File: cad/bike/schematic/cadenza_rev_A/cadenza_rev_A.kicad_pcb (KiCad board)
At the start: 2 copper layers, 90 x 60 mm, 60 parts, among them J2 USB_C_Receptacle, J3 Conn_01x02, J4 Conn_01x02, J5 Conn_01x02, Q1 BC547, SW1 SW_Slide_DPDT, SW2 SW_Push, SW3 SW_Push, U1 TLC5916, U10 HDSP-A151, U11 TLC5916, U12 HDSP-A151, U13 STM32F105RCTx, U14 LT1962-3.3, U15 TLC5916, U2 HDSP-A151, U3 TLC5916, U4 HDSP-A151, U5 TLC5916, U6 HDSP-A151, U7 TLC5916, U8 HDSP-A151, U9 TLC5916

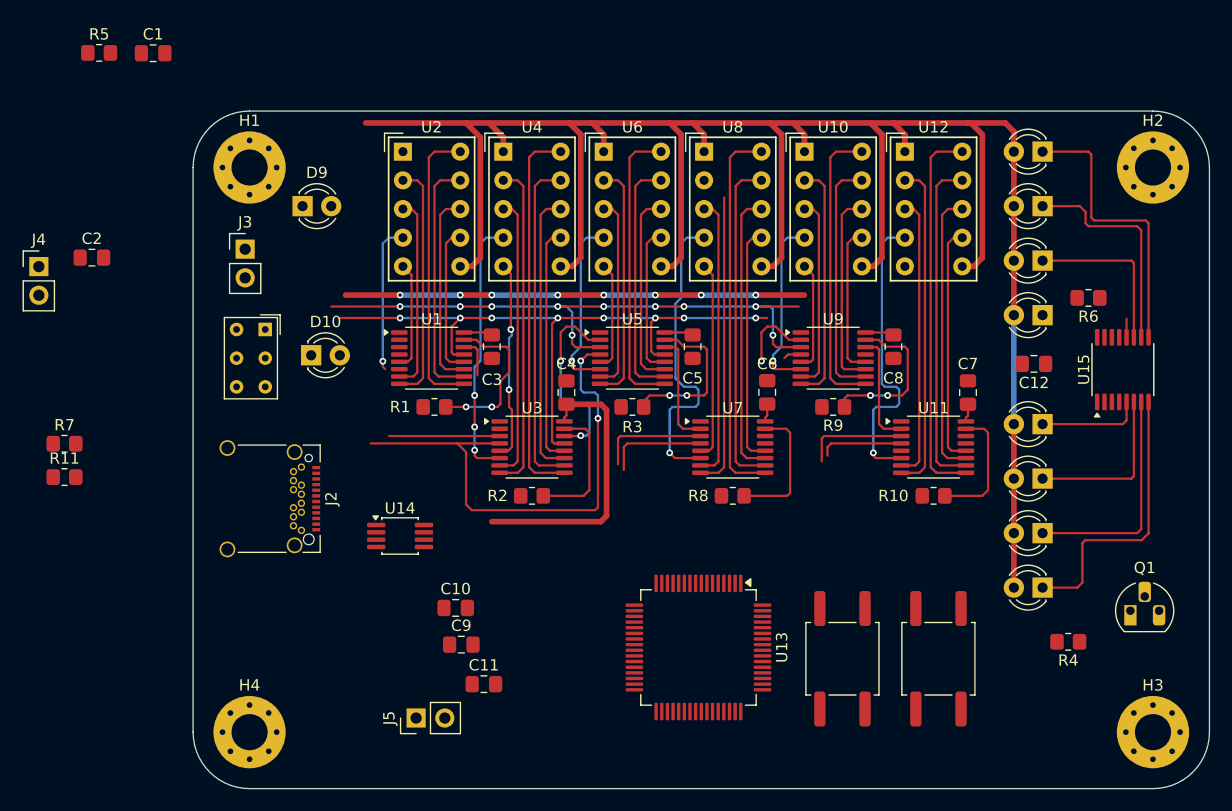
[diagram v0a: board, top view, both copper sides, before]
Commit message: added the debug interface
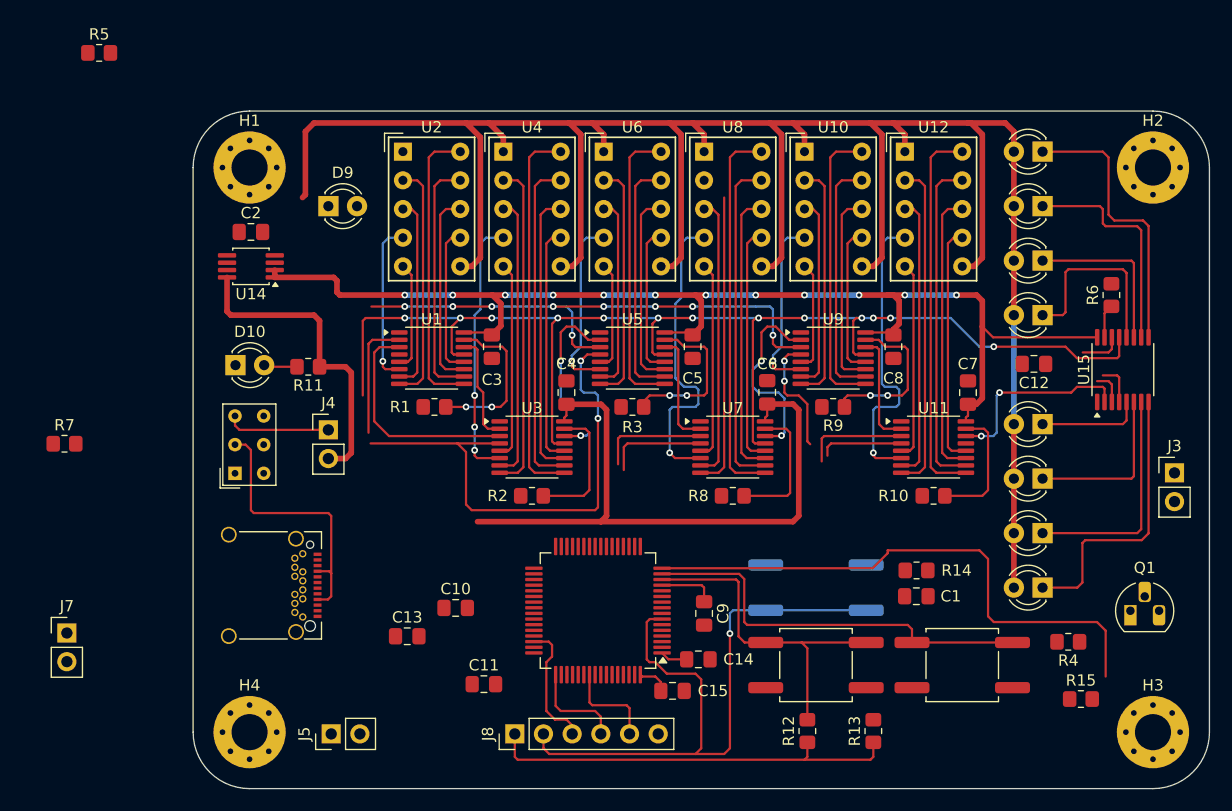
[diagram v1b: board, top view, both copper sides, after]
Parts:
- added C13: 10nF, Capacitor_SMD:C_0805_2012Metric_Pad1.18x1.45mm_HandSolder, F.Cu at (69.0, 96.5)
- added C14: 100nF, Capacitor_SMD:C_0805_2012Metric_Pad1.18x1.45mm_HandSolder, F.Cu at (94.7, 98.6)
- added C15: 100nF, Capacitor_SMD:C_0805_2012Metric_Pad1.18x1.45mm_HandSolder, F.Cu at (92.5, 101.3)
- added J7: Conn_01x02, Connector_PinHeader_2.54mm:PinHeader_1x02_P2.54mm_Vertical, F.Cu at (38.8, 96.2)
- added J8: Conn_01x06, Connector_PinHeader_2.54mm:PinHeader_1x06_P2.54mm_Vertical, F.Cu at (78.5, 105.2)
- added R12: R_US, Resistor_SMD:R_0805_2012Metric_Pad1.20x1.40mm_HandSolder, F.Cu at (104.4, 104.9)
- added R13: R_US, Resistor_SMD:R_0805_2012Metric_Pad1.20x1.40mm_HandSolder, F.Cu at (110.2, 104.9)
- added R14: 10k, Resistor_SMD:R_0805_2012Metric_Pad1.20x1.40mm_HandSolder, F.Cu at (114.1, 90.7)
- added R15: 1k, Resistor_SMD:R_0805_2012Metric_Pad1.20x1.40mm_HandSolder, F.Cu at (128.6, 102.1)
- added SW4: SW_Push, Button_Switch_SMD:SW_Push_1P1T_NO_CK_KSC6xxG, B.Cu at (105.2, 92.2)
- R5: value R_US -> 10k
- moved J3 84.6 mm to (136.9, 82.0)
- moved C1 82.9 mm to (114.0, 93.0)
- moved J4 29.4 mm to (62.0, 78.2)
- moved U14 27.3 mm to (55.1, 63.8), turned to 180 degrees
- moved R11 23.7 mm to (60.2, 72.6), turned to 180 degrees
- moved C9 21.7 mm to (95.2, 94.5), turned to -90 degrees
- moved C2 14.3 mm to (55.1, 60.7)
- moved SW1 13.0 mm to (53.7, 82.1), turned to 90 degrees
- moved U13 9.48 mm to (85.9, 94.2), turned to 180 degrees
- moved J2 7.67 mm to (56.0, 92.0)
- moved J5 7.65 mm to (62.2, 105.2)
- moved D10 6.76 mm to (53.8, 72.5)
- moved SW2 2.41 mm to (105.2, 99.1), turned to 180 degrees
- moved D9 2.29 mm to (62.0, 58.4)
- moved SW3 2.18 mm to (118.1, 99.1), turned to 180 degrees
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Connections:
- C1 pad 1: +3.3V -> /~{RESET}
- D1 pad 2: +5VL -> +5V
- D2 pad 2: +5VL -> +5V
- D3 pad 2: +5VL -> +5V
- D4 pad 2: +5VL -> +5V
- D5 pad 2: +5VL -> +5V
- D6 pad 2: +5VL -> +5V
- D7 pad 2: +5VL -> +5V
- D8 pad 2: +5VL -> +5V
- Q1 pad 2: unconnected-(Q1-B-Pad2) -> Net-(Q1-B)
- SW2 pad 1: unconnected-(SW2-Pad1) -> GND
- SW2 pad 2: unconnected-(SW2-Pad2) -> /PB_{1}
- SW3 pad 1: unconnected-(SW3-Pad1) -> GND
- SW3 pad 2: unconnected-(SW3-Pad2) -> /PB_{2}
- U10 pad 1: +5VL -> +5V
- U10 pad 6: +5VL -> +5V
- U12 pad 1: +5VL -> +5V
- U12 pad 6: +5VL -> +5V
- U13 pad 14: unconnected-(U13-PA0-Pad14) -> /PB_{1}
- U13 pad 15: unconnected-(U13-PA1-Pad15) -> /PB_{2}
- U13 pad 16: unconnected-(U13-PA2-Pad16) -> Net-(U13-PA2)
- U13 pad 46: unconnected-(U13-PA13-Pad46) -> /SW_DIO
- U13 pad 49: unconnected-(U13-PA14-Pad49) -> /SW_CLK
- U13 pad 55: unconnected-(U13-PB3-Pad55) -> /SW_O
- U13 pad 7: +3.3V -> /~{RESET}
- U14 pad 2: unconnected-(U14-SENSE-Pad2) -> +3.3V
- U14 pad 3: unconnected-(U14-BYP-Pad3) -> Net-(U14-BYP)
- U14 pad 5: unconnected-(U14-~{SHDN}-Pad5) -> +5V
- U2 pad 1: +5VL -> +5V
- U2 pad 6: +5VL -> +5V
- U4 pad 1: +5VL -> +5V
- U4 pad 6: +5VL -> +5V
- U6 pad 1: +5VL -> +5V
- U6 pad 6: +5VL -> +5V
- U8 pad 1: +5VL -> +5V
- U8 pad 6: +5VL -> +5V
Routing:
- net +5V: track 0.00 -> 239.7 mm
- net +5VL: track 200.1 -> 0.00 mm
- net +3.3V: track 37.2 -> 212.6 mm, vias 0 -> 12
- net /~{RESET}: track 0.00 -> 59.5 mm, vias 0 -> 1
- net Net-(U1-~{OE}(ED2)): track 59.1 -> 115.2 mm, vias 8 -> 13
- net Net-(U13-PA2): track 0.00 -> 50.1 mm
- net (no net): track 40.6 -> 0.00 mm, vias 8 -> 0
- net /PB_{2}: track 0.00 -> 36.5 mm
- net /PB_{1}: track 0.00 -> 30.3 mm
- net Net-(J2-VBUS-PadA4): track 0.00 -> 24.0 mm
- net Net-(U11-~{OUT0}): track 0.00 -> 17.5 mm
- net Net-(U11-SDO): track 0.00 -> 17.4 mm, vias 0 -> 2
- net Net-(D4-K): track 1.64 -> 17.0 mm
- net Net-(U1-LE(ED1)): track 63.3 -> 76.1 mm, vias 2 -> 4
- net /SW_DIO: track 0.00 -> 11.4 mm
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
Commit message: routing backup
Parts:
- added C16: 100nF, Capacitor_SMD:C_0805_2012Metric_Pad1.18x1.45mm_HandSolder, F.Cu at (104.4, 104.6)
- added C17: 100nF, Capacitor_SMD:C_0805_2012Metric_Pad1.18x1.45mm_HandSolder, F.Cu at (118.1, 104.7)
- added C18: 100nF, Capacitor_SMD:C_0805_2012Metric_Pad1.18x1.45mm_HandSolder, F.Cu at (67.3, 101.1)
- added C19: 100nF, Capacitor_SMD:C_0805_2012Metric_Pad1.18x1.45mm_HandSolder, F.Cu at (92.8, 87.9)
- added R16: 330, Resistor_SMD:R_0805_2012Metric_Pad1.20x1.40mm_HandSolder, F.Cu at (63.2, 62.2)
- R12, R13, R7: value R_US -> 4.7k
- moved R5 59.8 mm to (74.7, 94.7)
- moved C13 35.6 mm to (59.2, 62.2), turned to 90 degrees
- moved R7 33.9 mm to (64.8, 101.1), turned to -90 degrees
- moved J7 31.6 mm to (70.4, 94.0), turned to -90 degrees
- moved R15 10.2 mm to (134.9, 94.0), turned to 90 degrees
- moved C12 7.20 mm to (129.0, 66.8), turned to 90 degrees
- moved C10 7.14 mm to (78.0, 88.6), turned to 180 degrees
- moved R11 6.20 mm to (55.1, 69.1), turned to 0 degrees
- moved Q1 5.77 mm to (134.4, 88.6), turned to 180 degrees
- moved J4 5.68 mm to (59.4, 73.2), turned to 180 degrees
- moved R13 5.59 mm to (115.8, 104.6)
- moved J3 5.57 mm to (131.8, 84.3), turned to 90 degrees
- moved R4 5.06 mm to (131.6, 94.0), turned to -90 degrees
- moved C2 4.59 mm to (53.6, 65.0)
- moved J8 3.81 mm to (74.7, 105.2)
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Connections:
- D9 pad 2: unconnected-(D9-A-Pad2) -> Net-(D9-A)
- J5 pad 1: +3.3V -> Net-(J5-Pin_1)
- R7 pad 1: Net-(J5-Pin_2) -> +3.3V
- R7 pad 2: GND -> Net-(J5-Pin_1)
- SW1 pad 2: Net-(J2-VBUS-PadA4) -> unconnected-(SW1-B-Pad2)
- SW1 pad 3: Net-(J4-Pin_1) -> unconnected-(SW1-C-Pad3)
- SW1 pad 5: unconnected-(SW1-B-Pad5) -> Net-(J2-VBUS-PadA4)
- SW1 pad 6: unconnected-(SW1-C-Pad6) -> Net-(J4-Pin_1)
- U1 pad 13: Net-(U1-~{OE}(ED2)) -> /~{LED_OUTPUT_EN}
- U1 pad 4: Net-(U1-LE(ED1)) -> /LED_LATCH_EN
- U11 pad 13: Net-(U1-~{OE}(ED2)) -> /~{LED_OUTPUT_EN}
- U11 pad 4: Net-(U1-LE(ED1)) -> /LED_LATCH_EN
- U13 pad 20: unconnected-(U13-PA4-Pad20) -> /LED_LATCH_EN
- U13 pad 33: unconnected-(U13-PB12-Pad33) -> /WARNING_LED
- U13 pad 35: unconnected-(U13-PB14-Pad35) -> /~{LED_OUTPUT_EN}
- U13 pad 40: unconnected-(U13-PC9-Pad40) -> Net-(J5-Pin_2)
- U15 pad 13: Net-(U1-~{OE}(ED2)) -> /~{LED_OUTPUT_EN}
- U15 pad 4: Net-(U1-LE(ED1)) -> /LED_LATCH_EN
- U3 pad 13: Net-(U1-~{OE}(ED2)) -> /~{LED_OUTPUT_EN}
- U3 pad 4: Net-(U1-LE(ED1)) -> /LED_LATCH_EN
- U5 pad 13: Net-(U1-~{OE}(ED2)) -> /~{LED_OUTPUT_EN}
- U5 pad 4: Net-(U1-LE(ED1)) -> /LED_LATCH_EN
- U7 pad 13: Net-(U1-~{OE}(ED2)) -> /~{LED_OUTPUT_EN}
- U7 pad 4: Net-(U1-LE(ED1)) -> /LED_LATCH_EN
- U9 pad 13: Net-(U1-~{OE}(ED2)) -> /~{LED_OUTPUT_EN}
- U9 pad 4: Net-(U1-LE(ED1)) -> /LED_LATCH_EN
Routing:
- net /~{LED_OUTPUT_EN}: track 0.00 -> 159.3 mm, vias 0 -> 14
- net /LED_LATCH_EN: track 0.00 -> 141.7 mm, vias 0 -> 9
- net Net-(U1-~{OE}(ED2)): track 115.2 -> 0.00 mm, vias 13 -> 0
- net +3.3V: track 212.6 -> 323.4 mm
- net Net-(U1-LE(ED1)): track 76.1 -> 0.00 mm, vias 4 -> 0
- net /SPI_CLK: track 90.6 -> 165.9 mm, vias 9 -> 14
- net /WARNING_LED: track 0.00 -> 41.3 mm, vias 0 -> 2
- net /SPI_MOSI: track 10.7 -> 39.6 mm, vias 0 -> 2
- net Net-(J7-Pin_1): track 0.00 -> 26.4 mm, vias 0 -> 2
- net +5V: track 239.7 -> 265.3 mm
- net Net-(J5-Pin_2): track 0.00 -> 23.4 mm, vias 0 -> 2
- net /PB_{2}: track 36.5 -> 45.5 mm
- net /~{RESET}: track 59.5 -> 51.8 mm
- net Net-(Q1-B): track 0.00 -> 4.56 mm
- net Net-(Q1-E): track 0.00 -> 4.46 mm
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
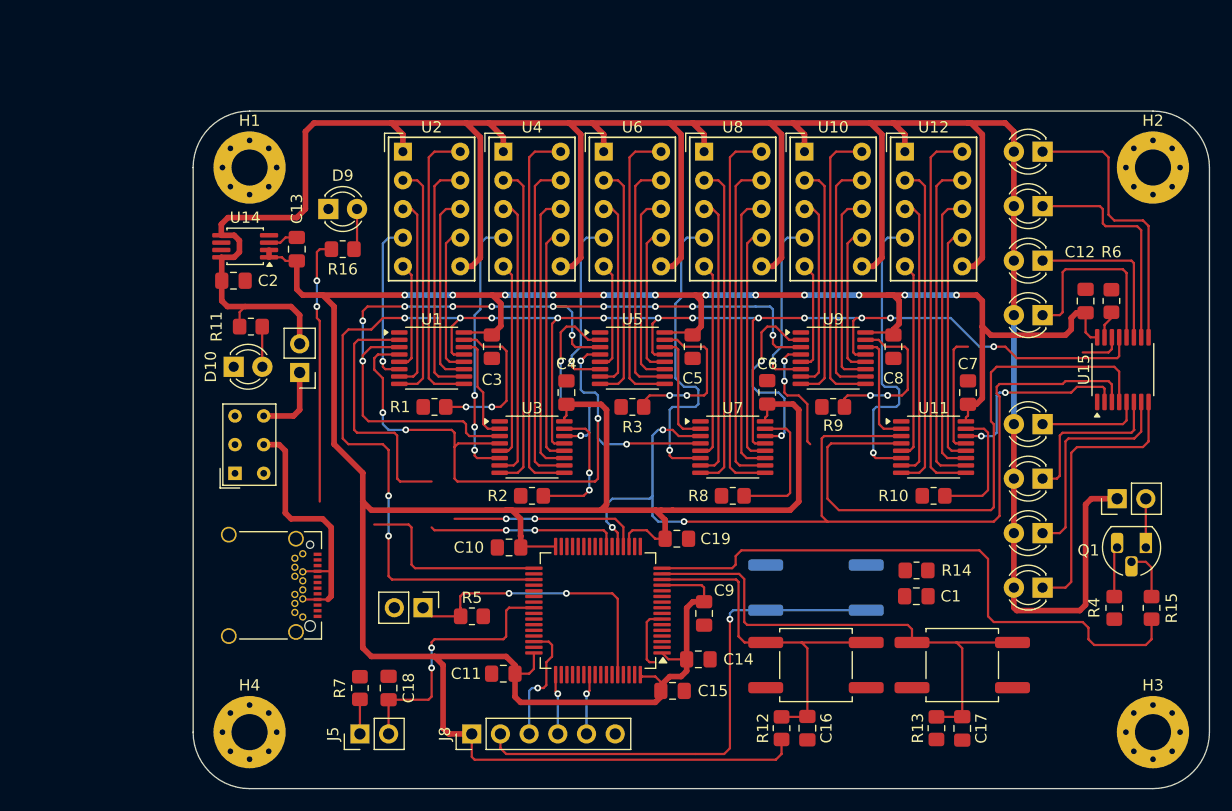
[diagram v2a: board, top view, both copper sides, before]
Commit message: finalised ground plane most of the routing done
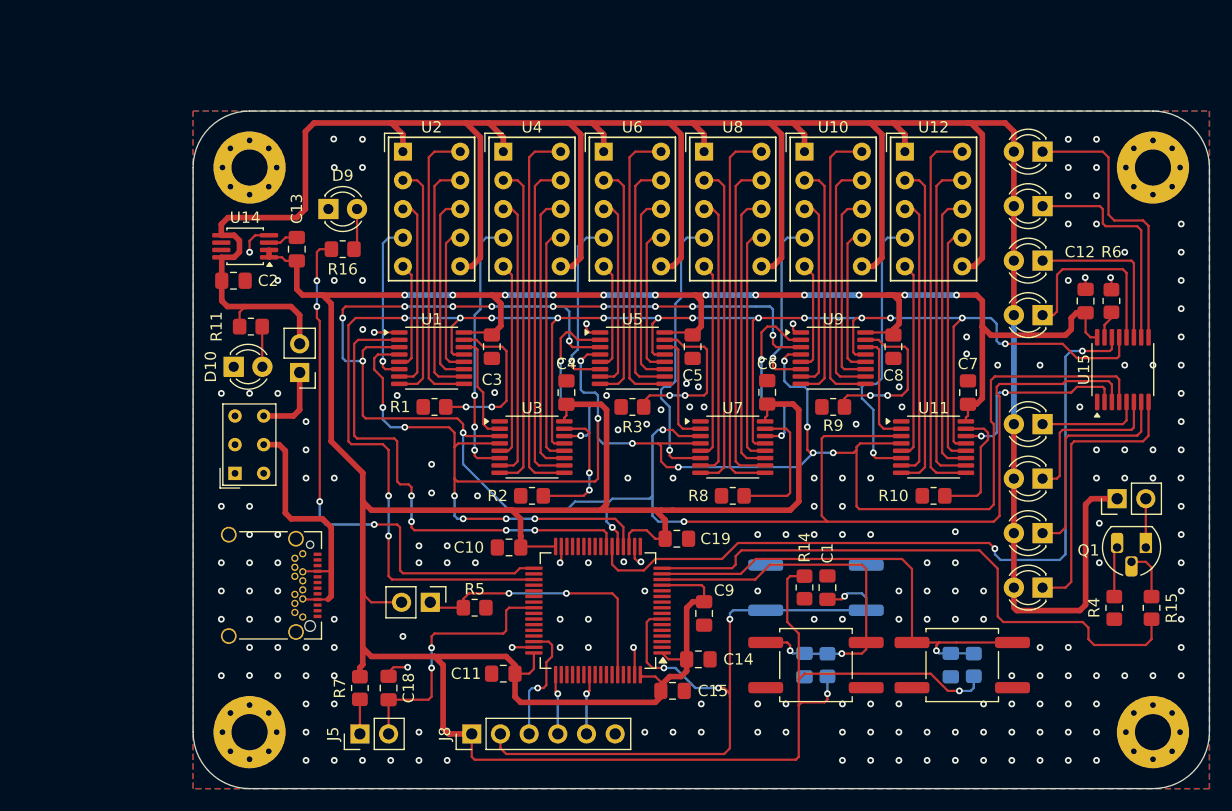
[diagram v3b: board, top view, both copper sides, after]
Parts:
- C16, C17, R12, R13: moved to B.Cu
- moved R14 10.0 mm to (104.1, 92.2), turned to -90 degrees
- moved C1 7.91 mm to (106.2, 92.2), turned to 90 degrees
- moved R12 6.91 mm to (106.2, 99.1)
- moved R13 6.50 mm to (119.1, 99.0)
- moved C17 5.70 mm to (117.1, 99.1)
- moved C16 5.59 mm to (104.1, 99.1)
- moved J7 0.80 mm to (71.0, 93.5)
- moved R5 0.80 mm to (74.9, 94.0)
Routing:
- net /SPI_MISO: track 3.75 -> 67.0 mm, vias 0 -> 2
- net +3.3V: track 323.4 -> 370.1 mm, vias 12 -> 14
- net /SPI_CLK: track 165.9 -> 187.3 mm, vias 14 -> 15
- net GND: track 0.00 -> 20.5 mm, vias 0 -> 200
- net /LED_LATCH_EN: track 141.7 -> 159.5 mm, vias 9 -> 14
- net /~{RESET}: track 51.8 -> 65.6 mm, vias 1 -> 4
- net /WARNING_LED: track 41.3 -> 48.5 mm, vias 2 -> 4
- net /SPI_MOSI: track 39.6 -> 43.5 mm, vias 2 -> 4
- net /PB_{1}: track 32.3 -> 35.6 mm, vias 0 -> 2
- net /PB_{2}: track 45.5 -> 42.7 mm, vias 0 -> 1
- net Net-(U7-~{OUT1}): track 27.7 -> 25.2 mm
- net /~{LED_OUTPUT_EN}: track 159.3 -> 161.6 mm, vias 14 -> 15
- net Net-(U11-~{OUT1}): track 26.8 -> 25.4 mm
- net Net-(J7-Pin_1): track 26.4 -> 25.5 mm
- net Net-(U7-SDO): track 17.4 -> 16.6 mm
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- added copper zone on B.Cu, net GND
- added copper zone on F.Cu, net GND

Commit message: added final touches, no more nets to route
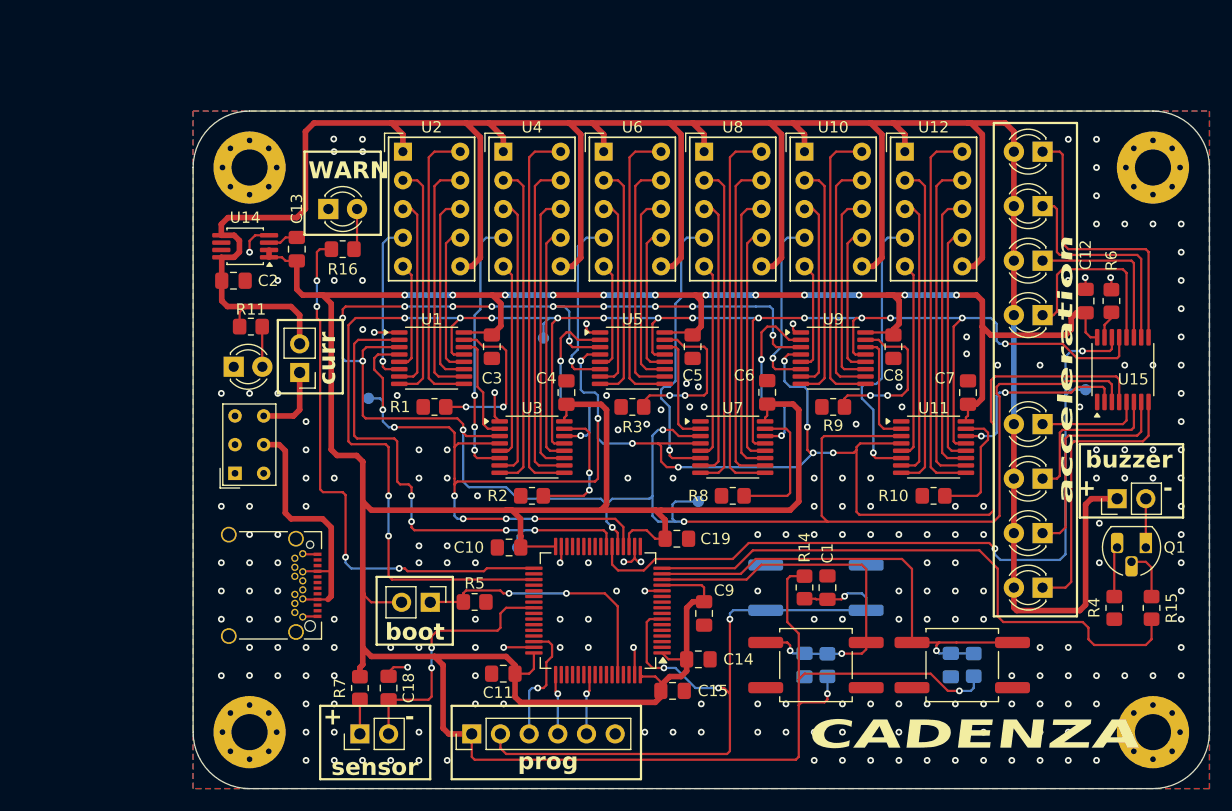
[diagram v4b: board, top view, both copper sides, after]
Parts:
- added TP1: TestPoint, TestPoint:TestPoint_Pad_D1.0mm, B.Cu at (94.7, 84.6)
- added TP2: TestPoint, TestPoint:TestPoint_Pad_D1.0mm, B.Cu at (78.7, 88.6)
- added TP3: TestPoint, TestPoint:TestPoint_Pad_D1.0mm, B.Cu at (65.5, 75.4)
- added TP4: TestPoint, TestPoint:TestPoint_Pad_D1.0mm, B.Cu at (81.0, 70.1)
- added TP5: TestPoint, TestPoint:TestPoint_Pad_D1.0mm, B.Cu at (129.0, 74.7)
- moved R5 0.51 mm to (74.9, 93.5)
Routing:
- net GND: track 20.5 -> 29.2 mm, vias 200 -> 214
- net /SPI_CLK: track 187.3 -> 191.8 mm
- net /LED_LATCH_EN: track 159.5 -> 162.7 mm
- net /~{LED_OUTPUT_EN}: track 161.6 -> 163.7 mm
- net /SPI_MISO: track 67.0 -> 69.0 mm
- net /SPI_MOSI: track 43.5 -> 45.3 mm
- net /~{RESET}: track 65.6 -> 66.8 mm
- net +3.3V: track 370.1 -> 371.1 mm
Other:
- board text added: "+"
- board text added: "-"
- board text added: "3V3"
- board text added: "CADENZA"
- board text added: "LATCH EN"
- board text added: "OUTPUT EN"
- board text added: "QuBi"
- board text added: "SPI CLK"
- board text added: "SPI MISO"
- board text added: "SPI MOSI"
- board text added: "WARN"
- board text added: "acceleration"
- board text added: "boot"
- board text added: "buzzer"
- board text added: "clk"
- board text added: "curr"
- board text added: "dio"
- board text added: "gnd"
- board text added: "jul 2026"
- board text added: "prog"
- board text added: "rev A"
- board text added: "rst"
- board text added: "sensor"
- board text added: "swo"
